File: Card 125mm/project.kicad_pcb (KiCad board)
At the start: 2 copper layers, 51.5 x 22 mm, 7 parts, among them J1 Molex PicoBlade, J2 Hirose DF13, J3 TestPoints, J4 TestPoints, U1 24LC32, X0 Card Edge

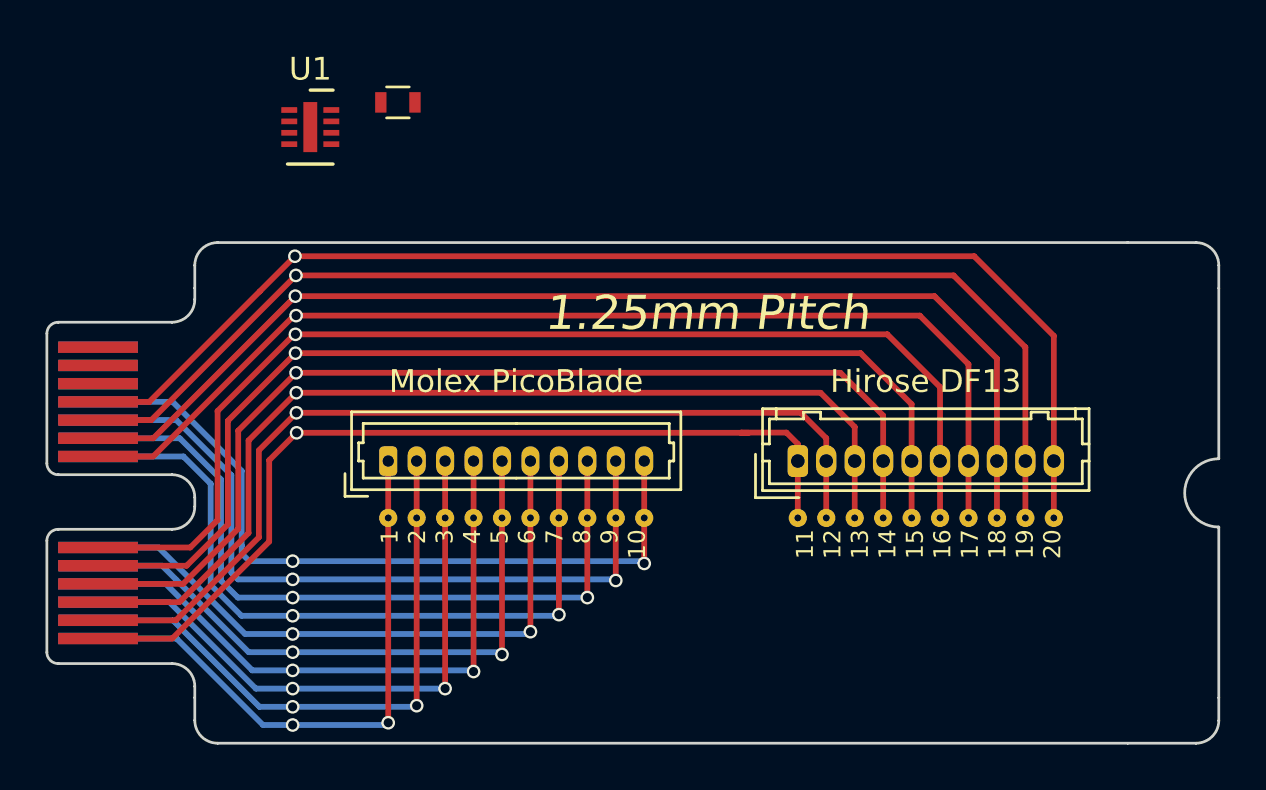
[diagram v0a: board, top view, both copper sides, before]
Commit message: EEPROM footprint update
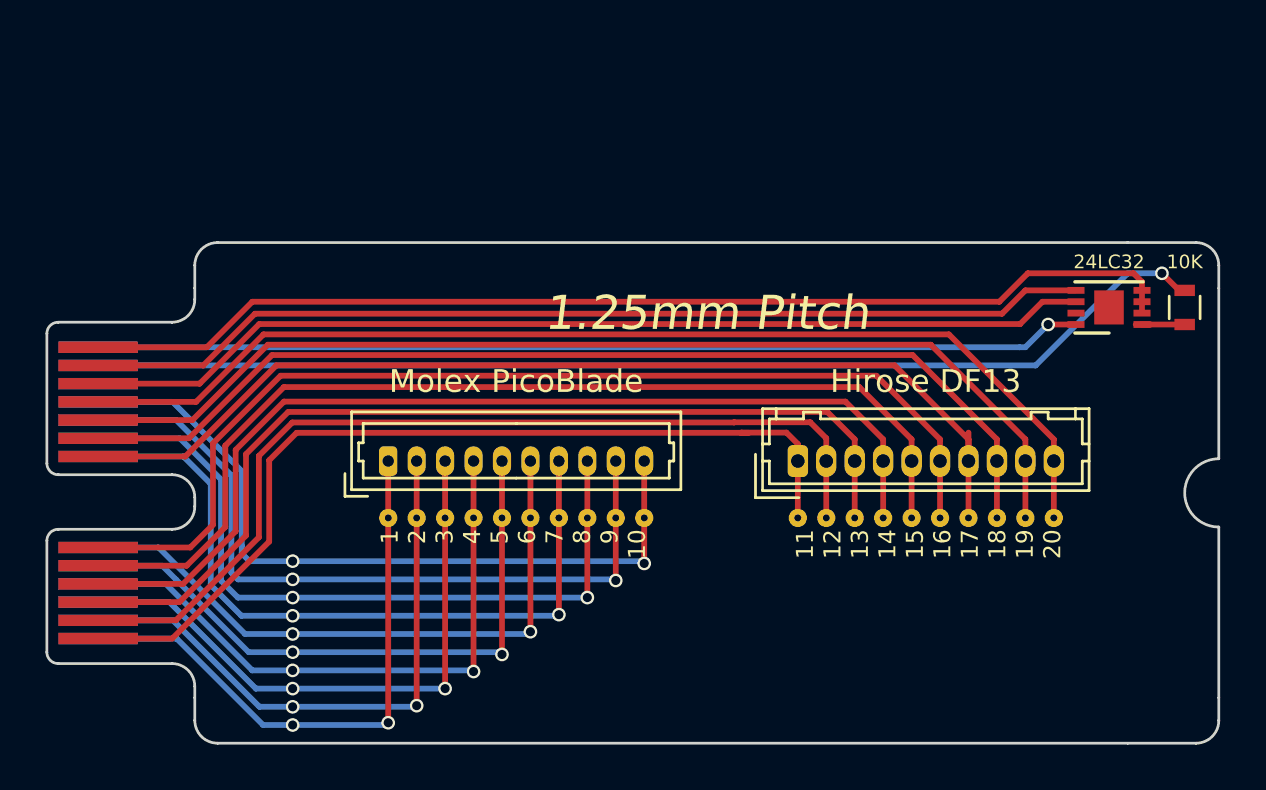
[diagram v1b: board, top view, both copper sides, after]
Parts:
- U1: footprint Package_DFN_QFN:DFN-8-1EP_2x3mm_P0.5mm_EP0.61x2.2mm -> Package_DFN_QFN:DFN-8-1EP_3x2mm_P0.5mm_EP1.3x1.5mm
- moved U1 36.0 mm to (46.7, -18.2), turned to 180 degrees
- moved R1 35.7 mm to (50.0, -18.2), turned to 90 degrees
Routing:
- net /A: track 0.00 -> 49.7 mm, vias 0 -> 1
- net GND: track 0.00 -> 48.8 mm
- net /D3_SCL: track 0.00 -> 44.5 mm
- net /D2_SDA: track 0.00 -> 44.3 mm
- net +5V: track 0.00 -> 43.4 mm, vias 0 -> 1
- net /20: track 54.1 -> 48.6 mm, vias 1 -> 0
- net /19: track 52.2 -> 47.3 mm, vias 1 -> 0
- net /18: track 50.2 -> 46.0 mm, vias 1 -> 0
- net /16: track 50.4 -> 46.8 mm, vias 1 -> 0
- net /15: track 48.2 -> 45.5 mm, vias 1 -> 0
- net Net-(R1-Pad1): track 0.00 -> 2.52 mm
- net /17: track 48.5 -> 46.0 mm, vias 1 -> 0
- net /14: track 46.1 -> 44.1 mm, vias 1 -> 0
- net /13: track 44.2 -> 42.8 mm, vias 1 -> 0
- net /12: track 42.0 -> 41.5 mm, vias 1 -> 0
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
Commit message: Updates
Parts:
- moved R1 2.02 mm to (48.0, -18.5)
- moved U1 1.69 mm to (45.0, -18.5)
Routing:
- net GND: track 48.8 -> 47.2 mm
- net /D2_SDA: track 44.3 -> 42.8 mm
- net /D3_SCL: track 44.5 -> 42.9 mm
- net +5V: track 43.4 -> 41.8 mm
- net Net-(R1-Pad1): track 2.52 -> 1.55 mm
- net /A: track 49.7 -> 49.2 mm
